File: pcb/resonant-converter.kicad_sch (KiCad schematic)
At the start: 20 parts, among them J1 Banana_Jack_Keystone_575-8, J2 Banana_Jack_Keystone_575-8, J3 Banana_Jack_Keystone_575-8, J4 Banana_Jack_Keystone_575-8, Q1 SIS472DN-T1-GE3, Q2 SIS472DN-T1-GE3, Q3 SIS472DN-T1-GE3, Q4 SIS472DN-T1-GE3, U1 UCC256610DDBR, U2 TEA2096T/1J

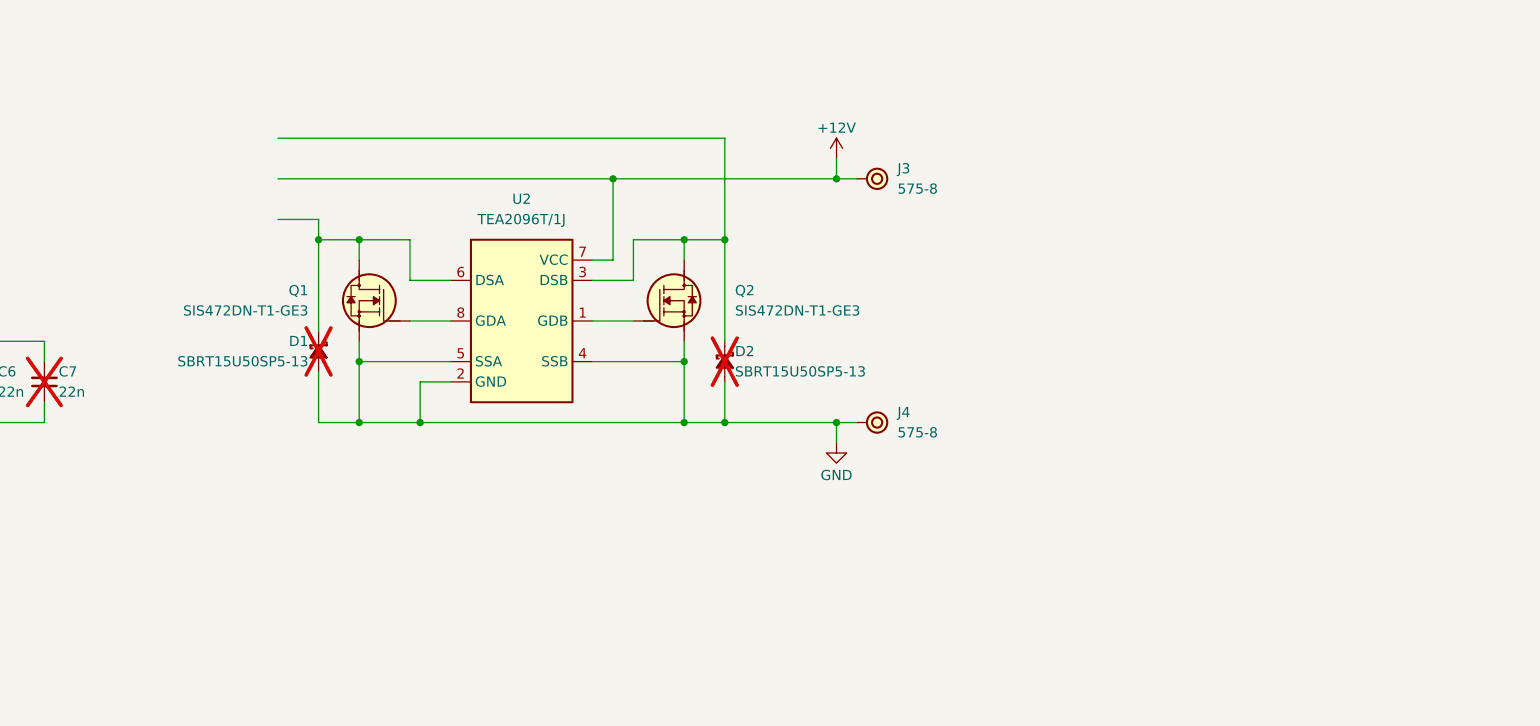
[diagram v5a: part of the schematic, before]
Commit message: [#4] Sch: Add INA219 power monitor
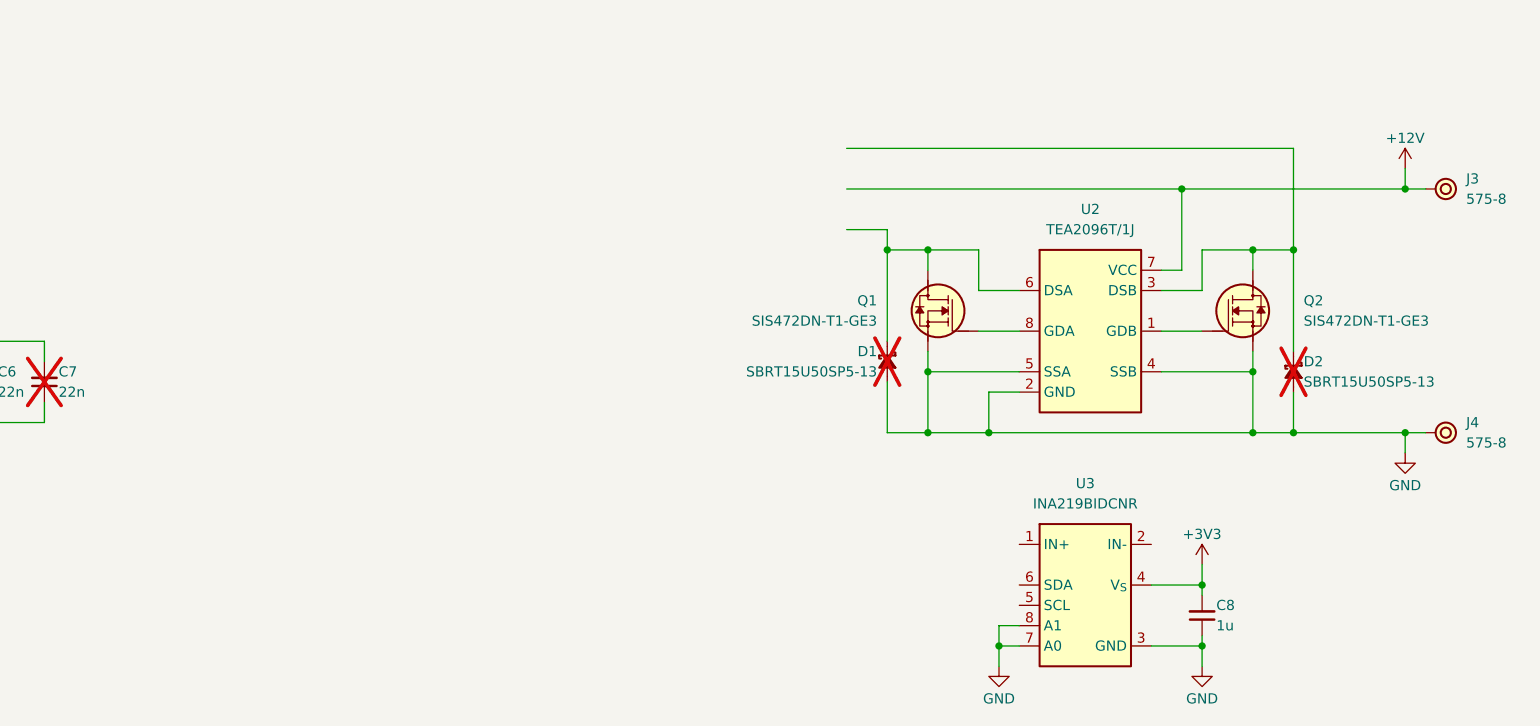
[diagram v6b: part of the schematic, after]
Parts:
- added C8: C-1u-0402, DW-footprints:C_0402_1005Metric, symbol DW-capacitors:C-1u-0402
- added U3: INA219BIDCNR, DW-footprints:SOT-23-8, symbol DW-ICs:INA219BIDCNR
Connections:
- net GND: now also C8.1, U3.3 (GND), U3.7 (A0), U3.8 (A1)
- new net +3V3: C8.2, U3.4 (V_{S})
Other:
- moved on the sheet: D1, D2, J3, J4, Q1, Q2, U2

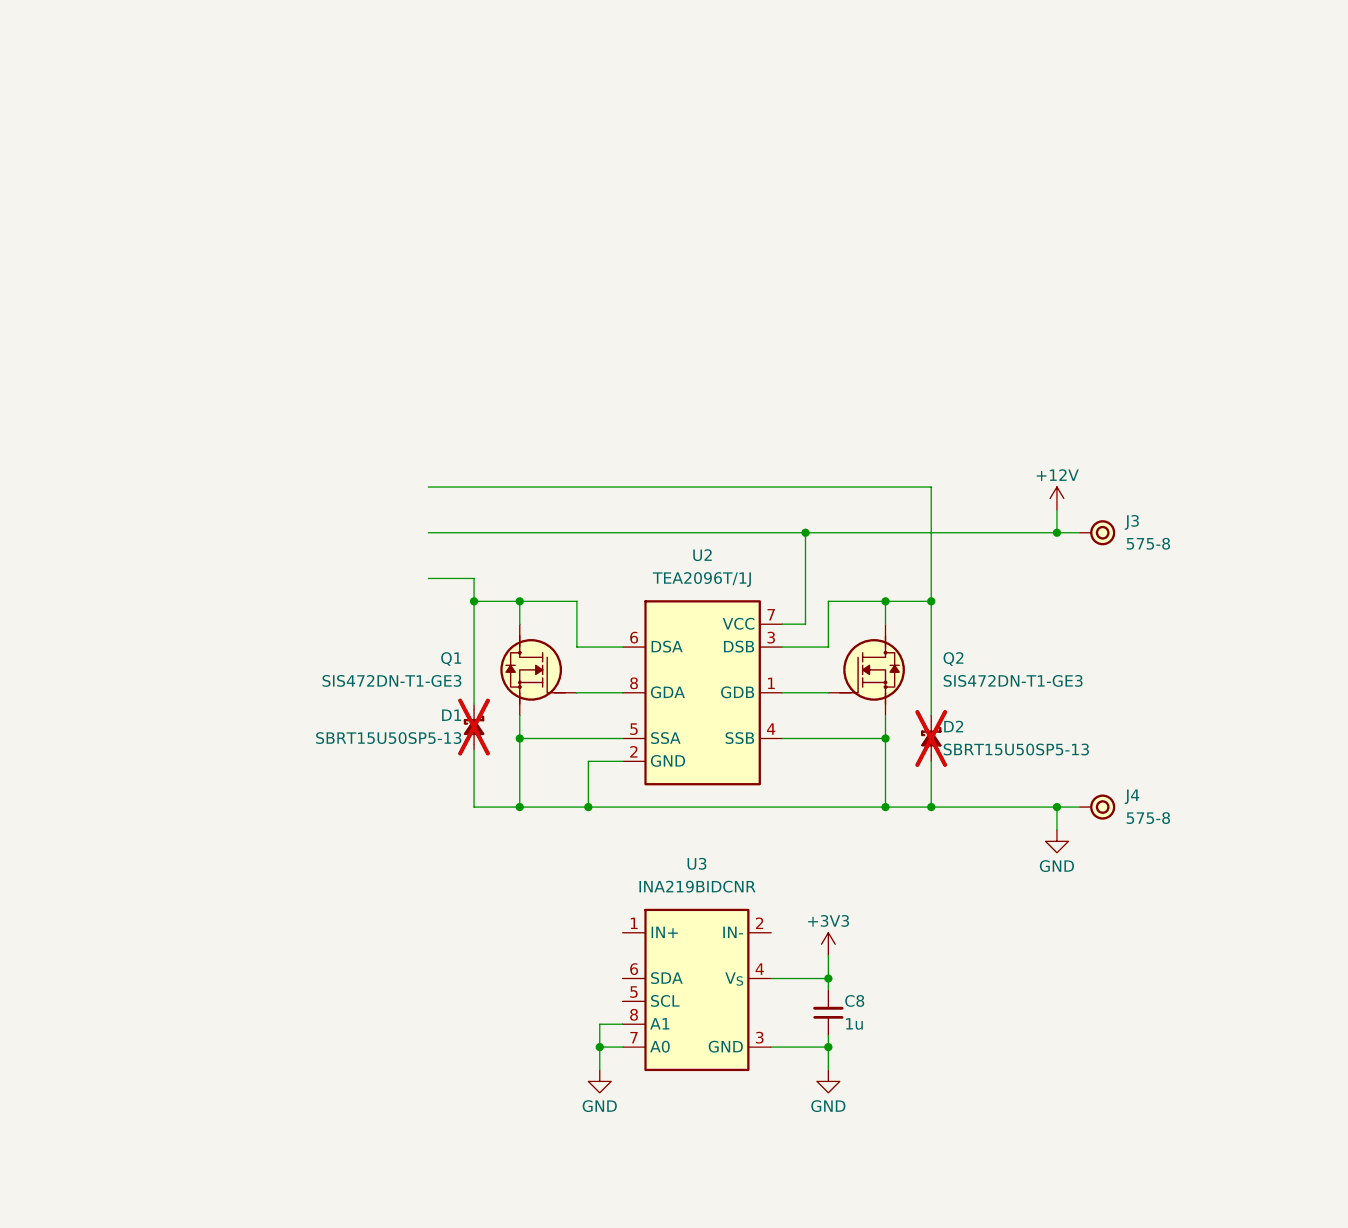
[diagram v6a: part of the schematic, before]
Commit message: [#4] Sch: Add transformer, draft feedback circuitry
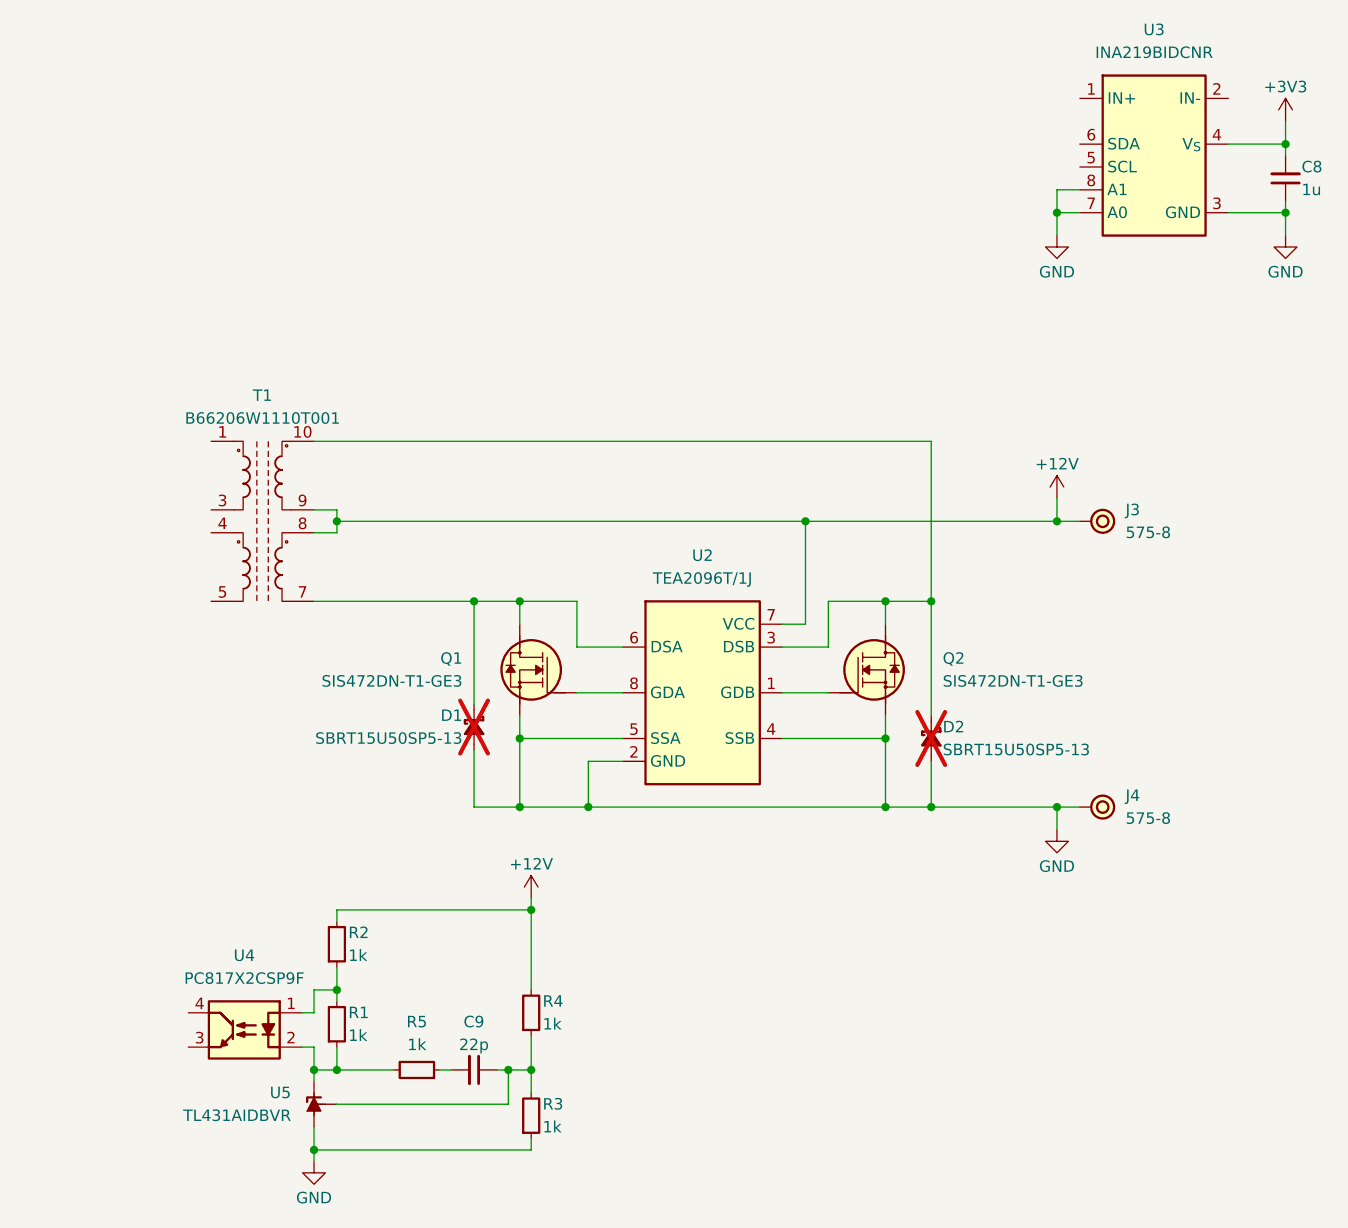
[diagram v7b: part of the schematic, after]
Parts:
- added C9: C-22p-0402, DW-footprints:C_0402_1005Metric, symbol DW-capacitors:C-22p-0402
- added R1, R2, R3, R4, R5: R-1k-0402, DW-footprints:R_0402_1005Metric, symbol DW-resistors:R-1k-0402
- added T1: B66206W1110T001, DW-footprints:Bobbin_B66206W1110T001, symbol DW-mechanical:Transformer_custom_B66206W1110T001
- added U4: PC817X2CSP9F, DW-footprints:SMD-4_6.5x4.6mm_P2.54mm, symbol DW-ICs:PC817X2CSP9F
- added U5: TL431AIDBVR, DW-footprints:SOT-23-5, symbol DW-ICs:TL431AIDBVR
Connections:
- net +12V: now also R2.2, R4.2, T1.8, T1.9
- net GND: now also R3.1, U5.5 (A)
- net at D2.1 (C), Q2.5 (D), U2.3 (DSB): now also T1.10
- net at D1.1 (C), Q1.5 (D), U2.6 (DSA): now also T1.7
- new net: C9.1, R3.2, R4.1, U5.4 (REF)
- new net: R1.1, R5.2, U4.2, U5.3 (K)
- new net: R1.2, R2.1, U4.1
- new net: C9.2, R5.1
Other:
- moved on the sheet: C8, J3, U3

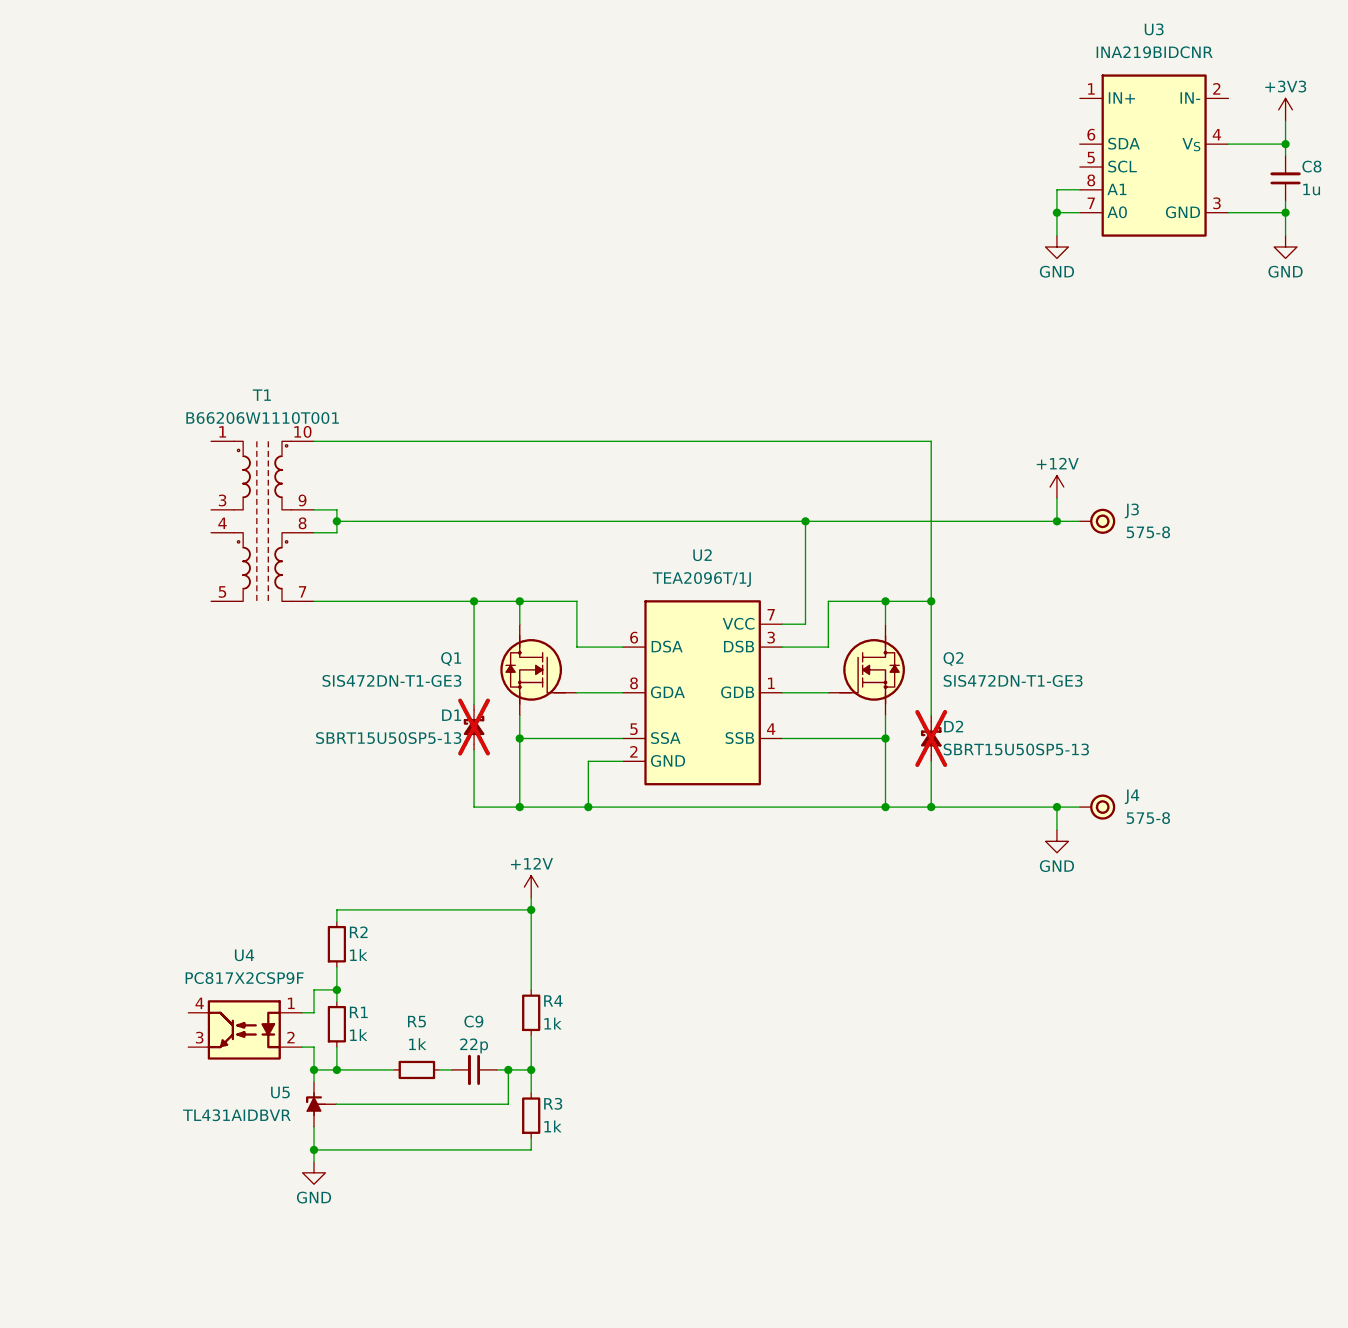
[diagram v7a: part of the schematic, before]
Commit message: [#4] Sch: Move INA219 power monitor to separate sheet, select initial feedback components values
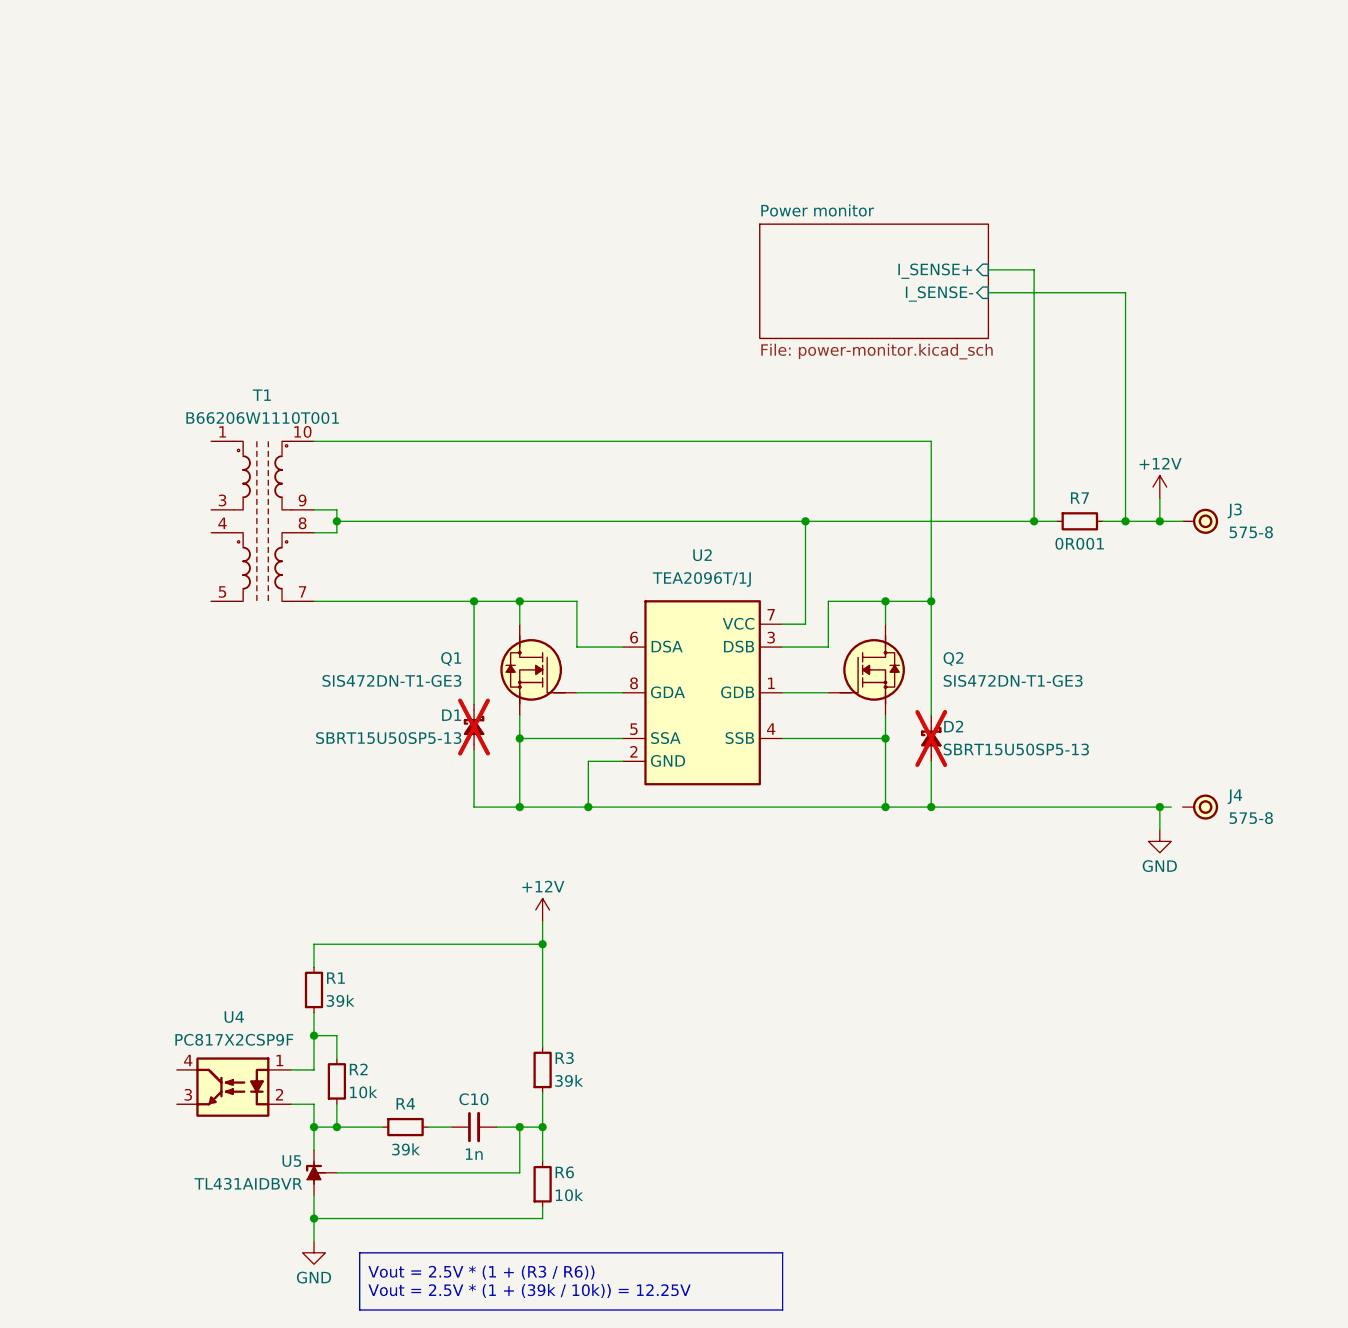
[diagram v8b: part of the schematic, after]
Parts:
- removed C8: C-1u-0402, DW-footprints:C_0402_1005Metric, symbol DW-capacitors:C-1u-0402
- removed C9: C-22p-0402, DW-footprints:C_0402_1005Metric, symbol DW-capacitors:C-22p-0402
- removed R1, R2, R3, R4, R5: R-1k-0402, DW-footprints:R_0402_1005Metric, symbol DW-resistors:R-1k-0402
- removed U3: INA219BIDCNR, DW-footprints:SOT-23-8, symbol DW-ICs:INA219BIDCNR
- added C10: C-1n-0402, DW-footprints:C_0402_1005Metric, symbol DW-capacitors:C-1n-0402
- added R1, R3, R4: R-39k-0402, DW-footprints:R_0402_1005Metric, symbol DW-resistors:R-39k-0402
- added R2, R6: R-10k-0402, DW-footprints:R_0402_1005Metric, symbol DW-resistors:R-10k-0402
- added R7: R-0R001-1206, DW-footprints:R_1206_3216Metric, symbol DW-resistors:R-0R001-1206
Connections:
- net +12V: now also R1.2, R3.2, R7.2; no longer T1.8, T1.9, U2.7 (VCC)
- net GND: now also R6.1; no longer J4.1
- net at U5.4 (REF): now also C10.2, R3.1, R6.2
- net at U4.2, U5.3 (K): now also R2.1, R4.1
- net at U4.1: now also R1.1, R2.2
- new net: C10.1, R4.2
- new net Power monitor/I_SENSE+: R7.1, T1.8, T1.9, U2.7 (VCC)
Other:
- added sheet Power monitor (power-monitor.kicad_sch)
- moved on the sheet: J3, J4, U4, U5
